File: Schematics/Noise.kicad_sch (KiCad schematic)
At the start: 28 parts, among them Q5 BC547, Q6 BC547, Q7 BC547, Q8 BC547

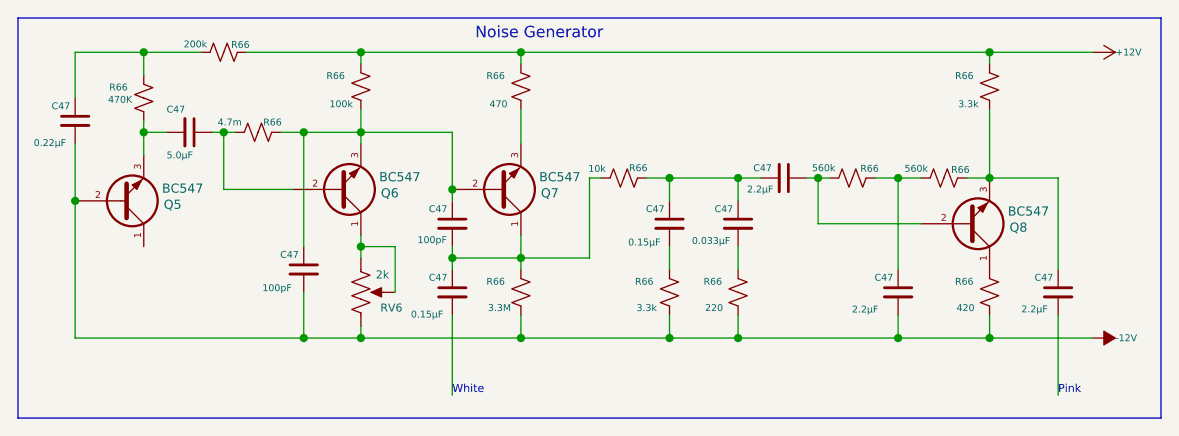
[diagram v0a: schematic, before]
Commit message: adding noise source and variable state filter.
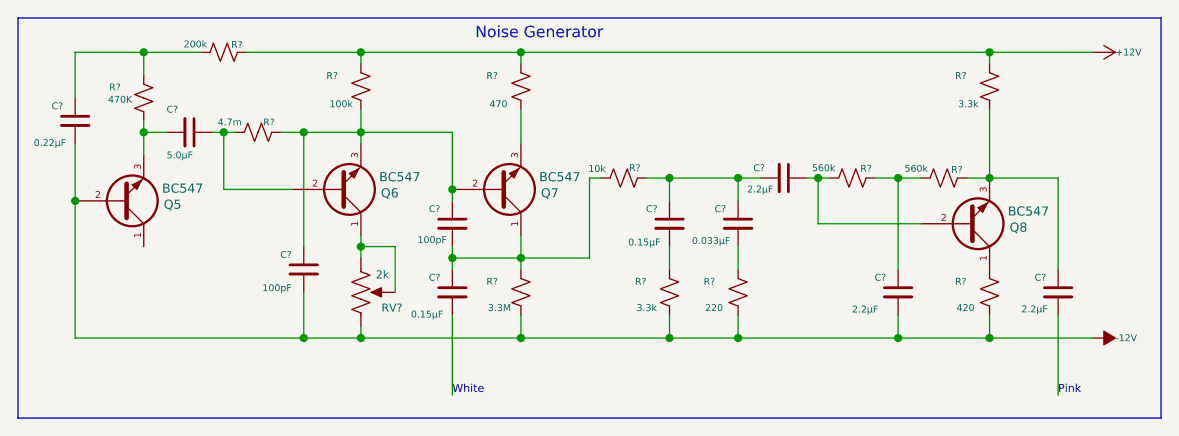
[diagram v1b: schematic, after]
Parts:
- renumbered C47 to C?, R66 to R?, RV6 to RV?

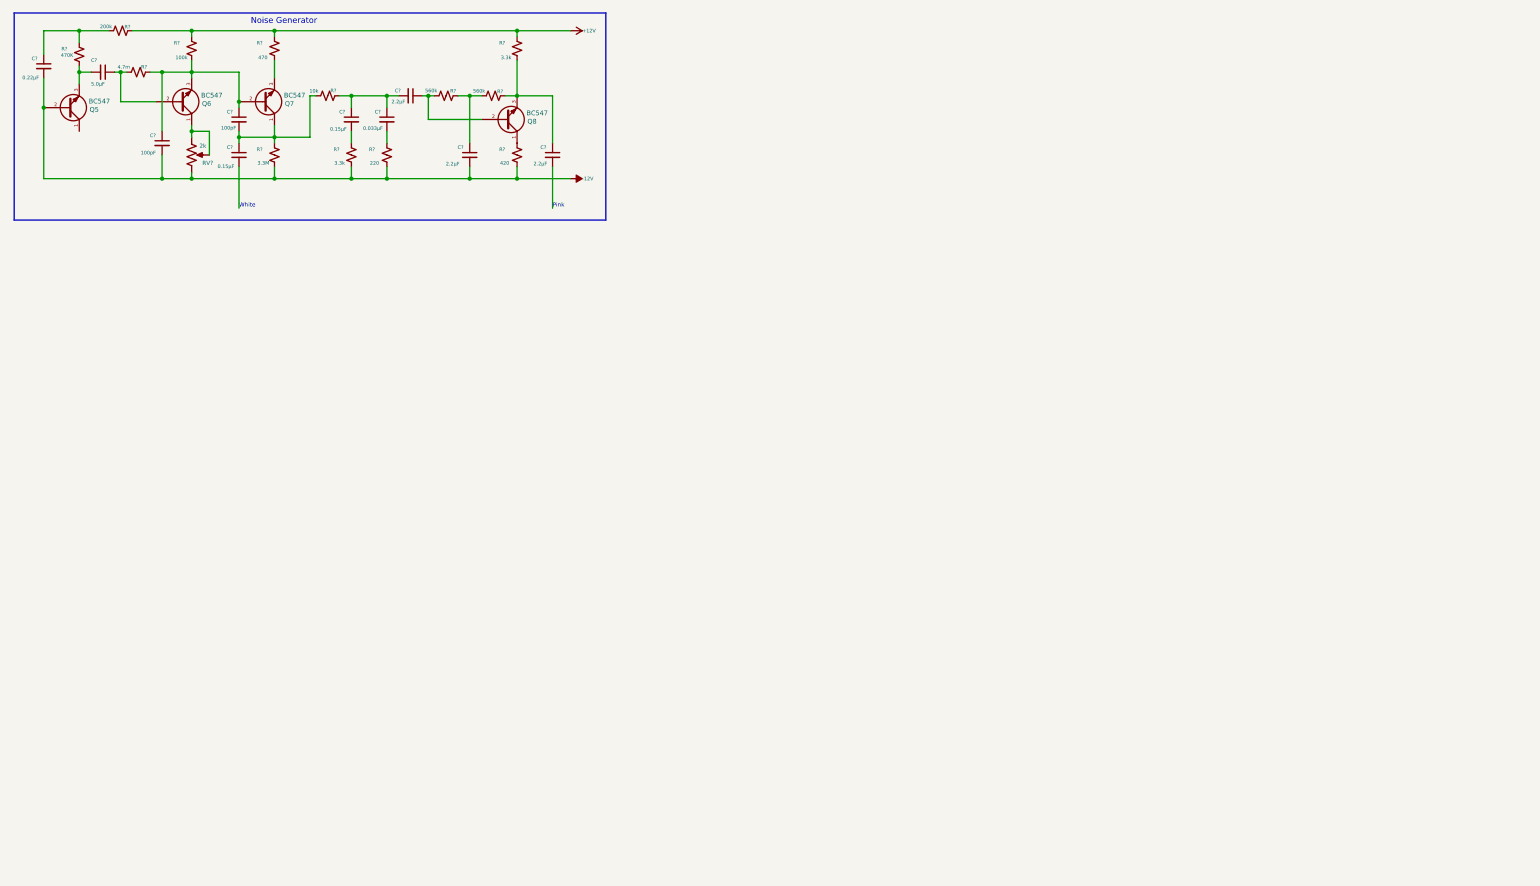
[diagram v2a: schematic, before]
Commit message: Update with noise filter & VCA as well as envelope generator software shell.
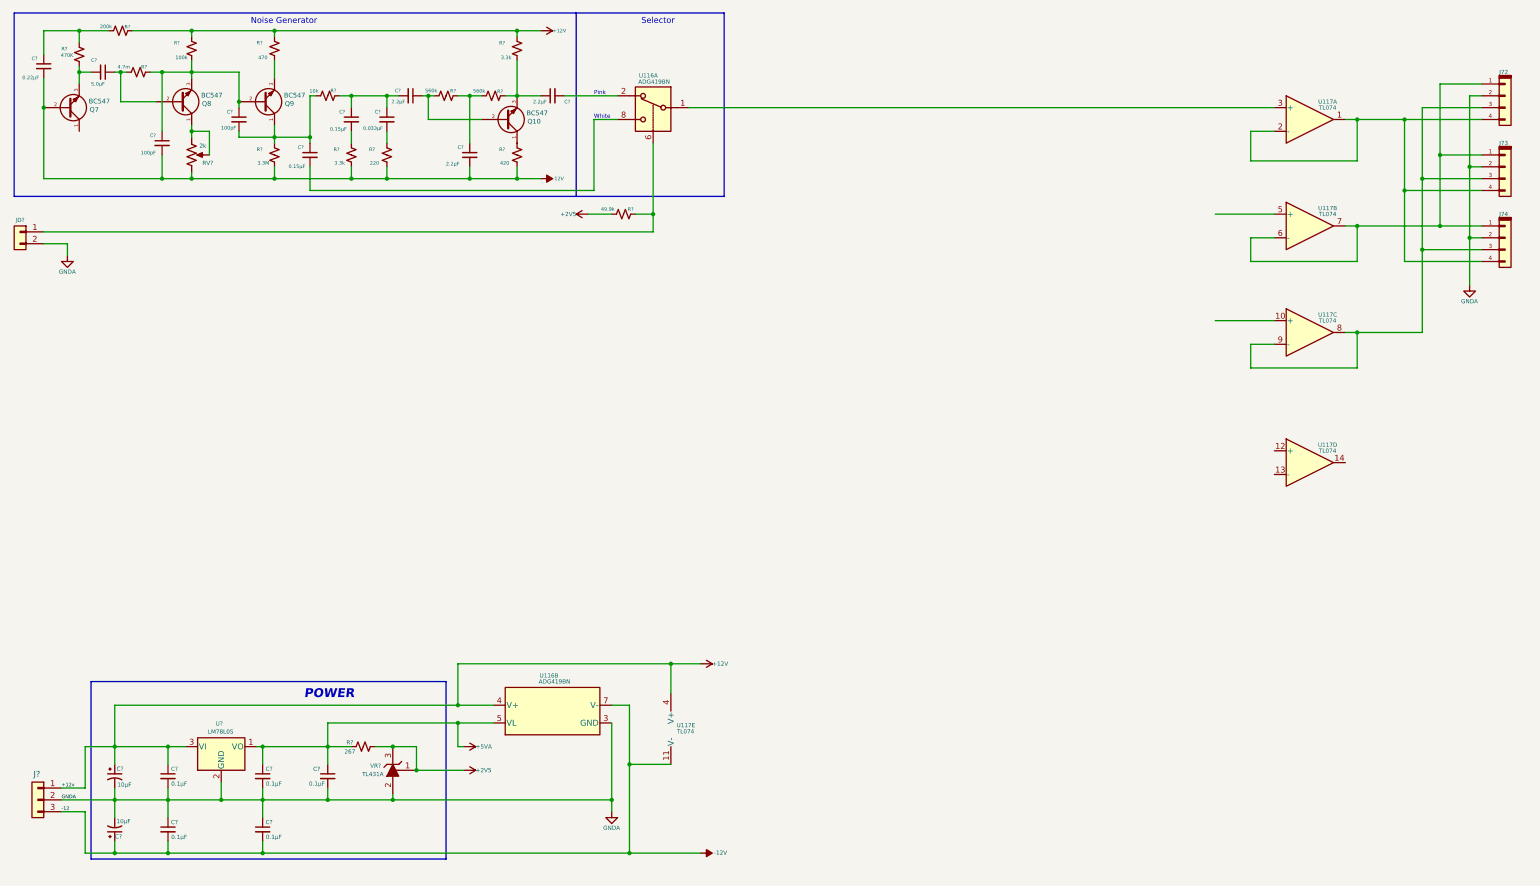
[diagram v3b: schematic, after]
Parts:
- added C? (x5): 0.1µF, symbol Device:C_Small
- added C? (x2): 10µF, symbol Device:C_Polarized_Small_US
- added J72, J73, J74: Conn_01x04, symbol Connector_keyed_kicad_sym:Conn_01x04
- added J?: Conn_01x03, symbol Connector_Generic:Conn_01x03
- added JD?: From 12v Analog, symbol Connector_Generic:Conn_01x02
- added R?: 267, symbol Device:R_Small_US
- added R?: 49.9k, symbol Device:R_Small_US
- added U116: ADG419BN, Package_DIP:DIP-8_W7.62mm, symbol Analog_Switch:ADG419BN
- added U117: TL074, symbol Amplifier_Operational:TL074
- added U?: LM78L05, Package_TO_SOT_THT:TO-92_Inline, symbol Regulator_Linear:LM78L05_TO92
- added VR?: TL431A, digikey-footprints:TO-92-3_Formed_Leads, symbol dk_PMIC-Voltage-Reference:TL431CLPM
- renumbered Q8 to Q10, Q5 to Q7, Q6 to Q8, Q7 to Q9
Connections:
- net +12V: now also C?.1, C?.1, J?.1 (Pin_1), U116.4 (V+), U117.4 (V+), U?.3 (VI)
- net -12V: now also C?.1, C?.2, C?.2, J?.3 (Pin_3), U116.7 (V-), U117.11 (V-)
- net at C?.2: now also U116.8
- net at C?.2: now also U116.2
- new net: J72.1 (Pin_1), J73.1 (Pin_1), J74.1 (Pin_1), U117.6 (-), U117.7
- new net: J72.3 (Pin_3), J73.3 (Pin_3), J74.3 (Pin_3), U117.8, U117.9 (-)
- new net: J72.4 (Pin_4), J73.4 (Pin_4), J74.4 (Pin_4), U117.1, U117.2 (-)
- new net: JD?.1 (Pin_1), R?.1, U116.6
- new net: U116.1, U117.3 (+)
- new net +2V5: R?.2, R?.2, VR?.1 (REF), VR?.3 (K)
- new net +5VA: C?.1, C?.1, R?.1, U116.5 (VL), U?.1 (VO)
- new net GNDA: C?.1, C?.1, C?.2, C?.2, C?.2, C?.2, C?.2, J72.2 (Pin_2), J73.2 (Pin_2), J74.2 (Pin_2), J?.2 (Pin_2), JD?.2 (Pin_2), U116.3 (GND), U?.2 (GND), VR?.2 (A)
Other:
- note added: "POWER"
- note added: "Selector"
- moved on the sheet: C?

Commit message: sync up first noise board.
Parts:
- removed JD?: From 12v Analog, symbol Connector_Generic:Conn_01x02
- removed R?: 200k, symbol Device:R_Small_US
- added J80, J81, J82: Conn_01x04, symbol Connector_keyed_kicad_sym:Conn_01x04
- added J84, J85: Conn_01x02, symbol Connector_keyed_kicad_sym:Conn_01x02
- added R124 (x12): 10k, symbol Device:R_Small_US
- added R142 (x6): 20k, symbol Device:R_Small_US
- added R148: 1k, symbol Device:R_Small_US
- added R?: 200K, symbol Device:R_Small_US
- added RV13: 100k, symbol Device:R_Potentiometer_US
- added U130, U131: TL074, symbol Amplifier_Operational:TL074
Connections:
- net +12V: now also R?.1, U130.4 (V+), U131.4 (V+)
- net -12V: now also U130.11 (V-), U131.11 (V-)
- net GNDA: now also J80.1 (Pin_1), J80.3 (Pin_3), J81.1 (Pin_1), J81.3 (Pin_3), J82.1 (Pin_1), J82.3 (Pin_3), J84.2 (Pin_2), J85.2 (Pin_2), U130.10 (+), U130.3 (+), U130.5 (+), U131.10 (+), U131.12 (+), U131.3 (+), U131.5 (+)
- net Filter Modulation: now reaches J72.1 (Pin_1), J73.1 (Pin_1), J74.1 (Pin_1), U117.6 (-), U117.7
- net VCA Modulation: now reaches J72.3 (Pin_3), J73.3 (Pin_3), J74.3 (Pin_3), U117.8, U117.9 (-)
- net Noise Out: now reaches J72.4 (Pin_4), J73.4 (Pin_4), J74.4 (Pin_4), U117.1, U117.2 (-)
- net at R?.1, U116.6: now also J85.1 (Pin_1)
- net at C?.1, R?.1: now also R?.2
- new net: R124.2, R142.1, U131.1
- new net: R124.1, R124.2, U131.2 (-)
- new net: R124.1, R124.2, U131.6 (-)
- new net: R124.2, R142.1, U131.7
- new net: R124.2, R142.1, U131.8
- new net: R142.2, R142.2, R142.2, R142.2, R142.2, R142.2, RV13. (3), U130.9 (-)
- new net: R124.2, R142.1, U131.14
- new net: J80.4 (Pin_4), R124.1
- new net: J82.4 (Pin_4), R124.1
- new net: R124.1, R124.2, U130.2 (-)
- new net: R124.1, R124.2, U131.9 (-)
- new net: R124.2, R142.1, U130.1
- new net: R124.2, R142.1, U130.7
- new net: R124.1, R124.2, U130.6 (-)
- new net: J82.2 (Pin_2), R124.1
- new net: J80.2 (Pin_2), R124.1
- new net: R148.1, RV13. (3), U130.8
- new net: R124.1, R124.2, U131.13 (-)
- new net: J81.4 (Pin_4), R124.1
- new net: J81.2 (Pin_2), R124.1
- new net To Mixer: J84.1 (Pin_1), R148.2
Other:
- note added: "Output"
- title: (none) -> Noise Generator and Mixer
- moved on the sheet: C?, J?, Q10, Q7, Q8, Q9, R?, RV?, U116A, U116B, U117A, U117B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

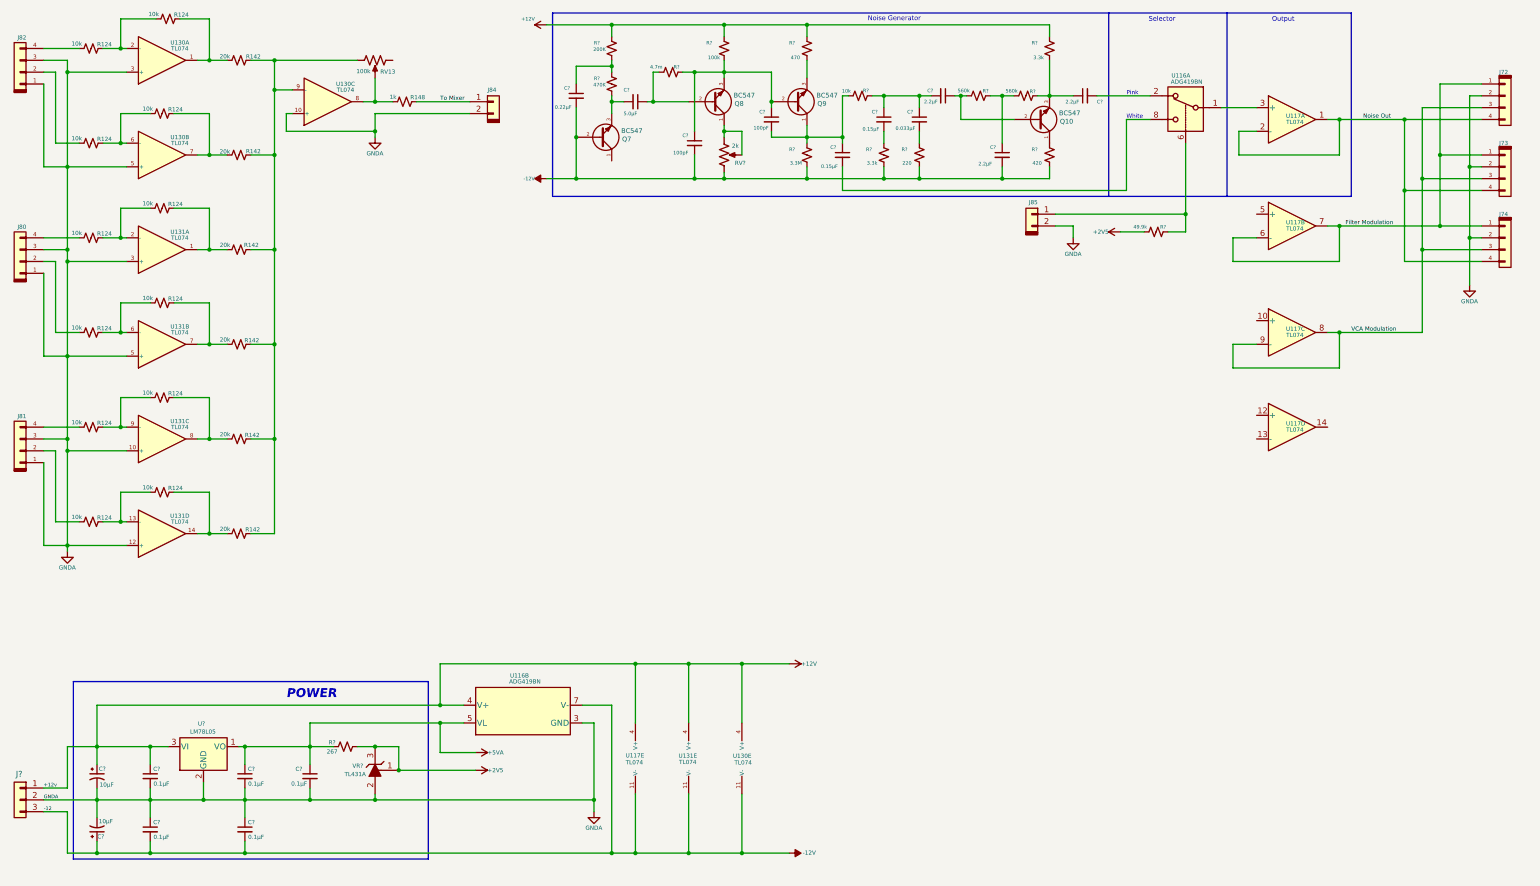
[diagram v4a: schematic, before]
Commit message: Partial software with complete hardware on best 3 state filter with 4 outputs.
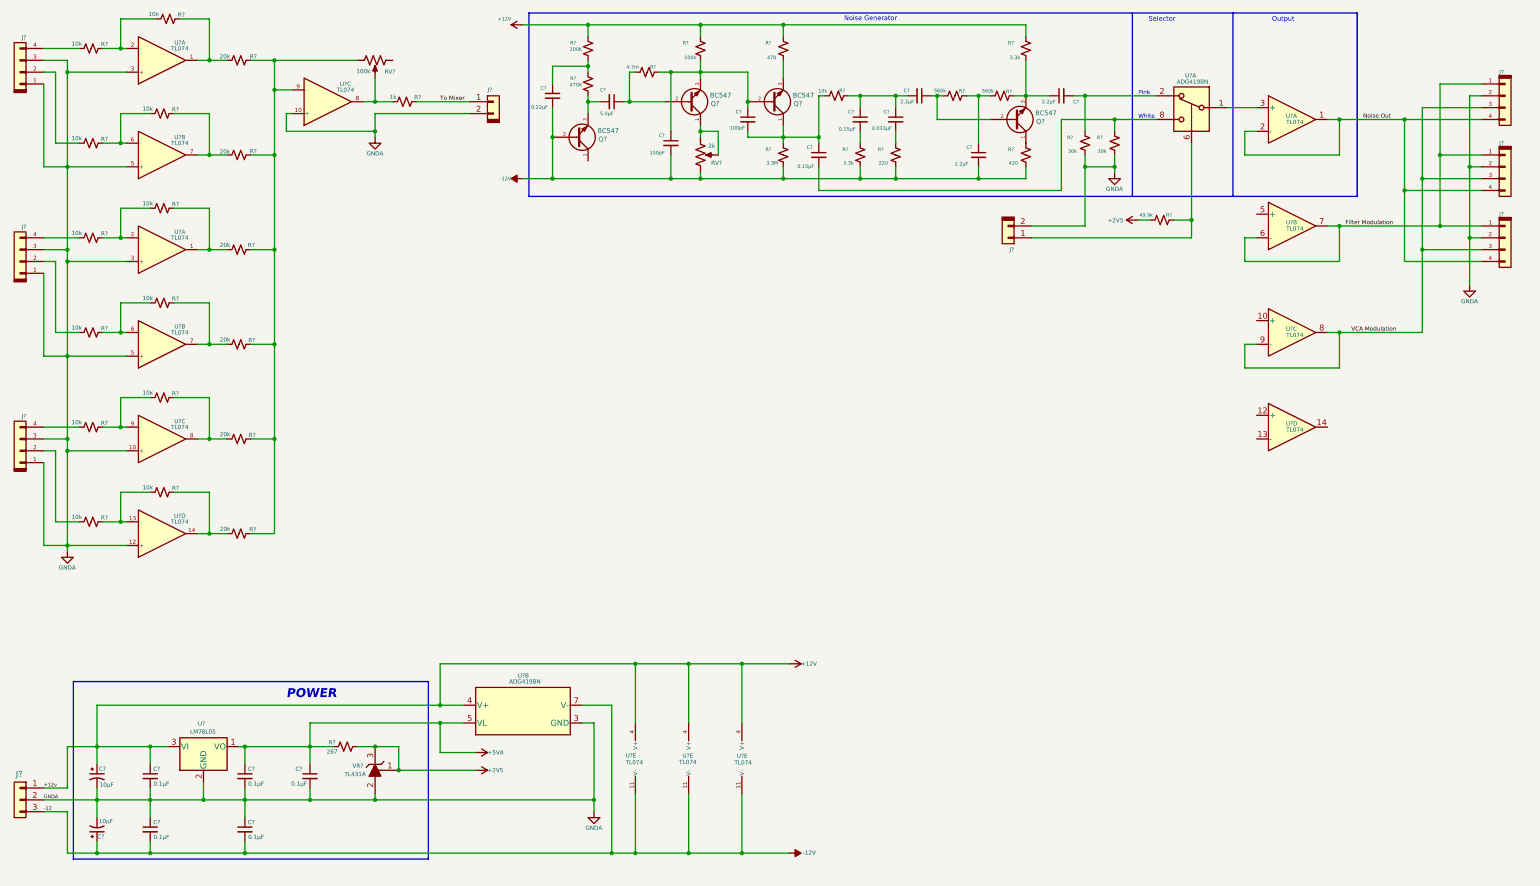
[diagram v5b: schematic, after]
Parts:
- added R? (x2): 30k, symbol Device:R_Small_US
- renumbered J73 to J?, J82 to J?, J80 to J?, J74 to J?, J84 to J?, J72 to J?, J85 to J?, J81 to J?, Q7 to Q?, Q9 to Q?, Q8 to Q?, Q10 to Q?, R142 to R?, R124 to R?, R148 to R?, RV13 to RV?, U131 to U?, U116 to U?, U117 to U?, U130 to U?
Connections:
- net GNDA: now also R?.2, R?.2
- net at C?.2, U?.8: now also R?.1
- net at C?.2, U?.2: now also R?.1
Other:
- moved on the sheet: C?, J?, Q?, R?, RV?, U?A

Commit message: - Updated current libraries - New 7 inc display with ESP32S3 and second USB upload port - Start of I2C feeder interface slave on display.
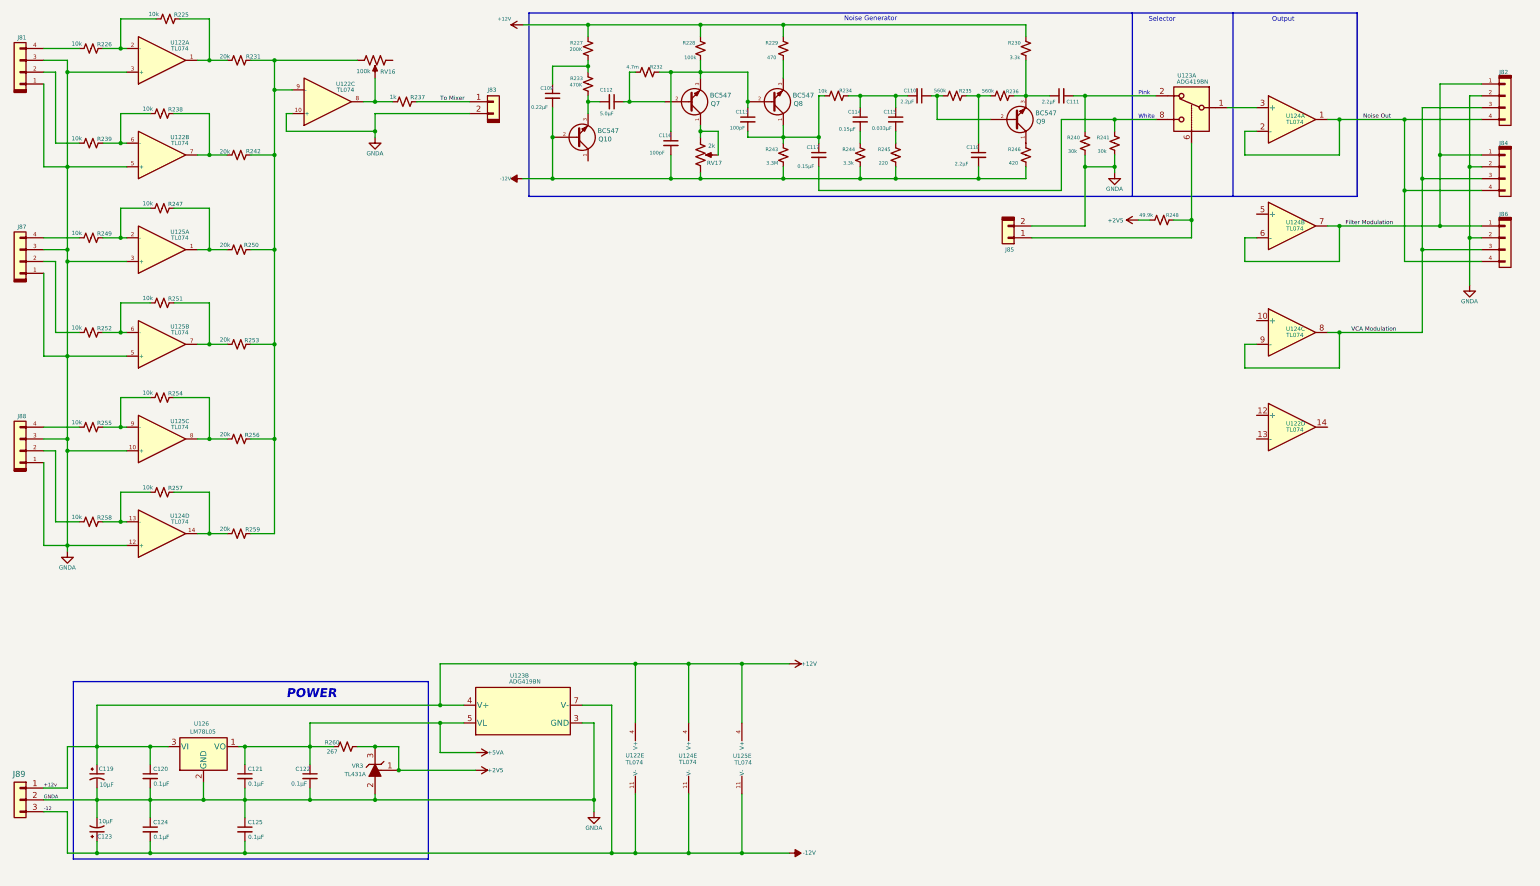
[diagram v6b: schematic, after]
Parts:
- gave numbers to parts that had none: 74
